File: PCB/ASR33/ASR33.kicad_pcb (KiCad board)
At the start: 2 copper layers, 45 x 27 mm, 44 parts, among them J1 Shelly, J2 DC, J3 Power, J4 RUN, J5 Tx, J6 Rx, J7 USB-C, Q1 NX7002AK, SW1 SW_Push, U1 ESP32-PICO-MINI-02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

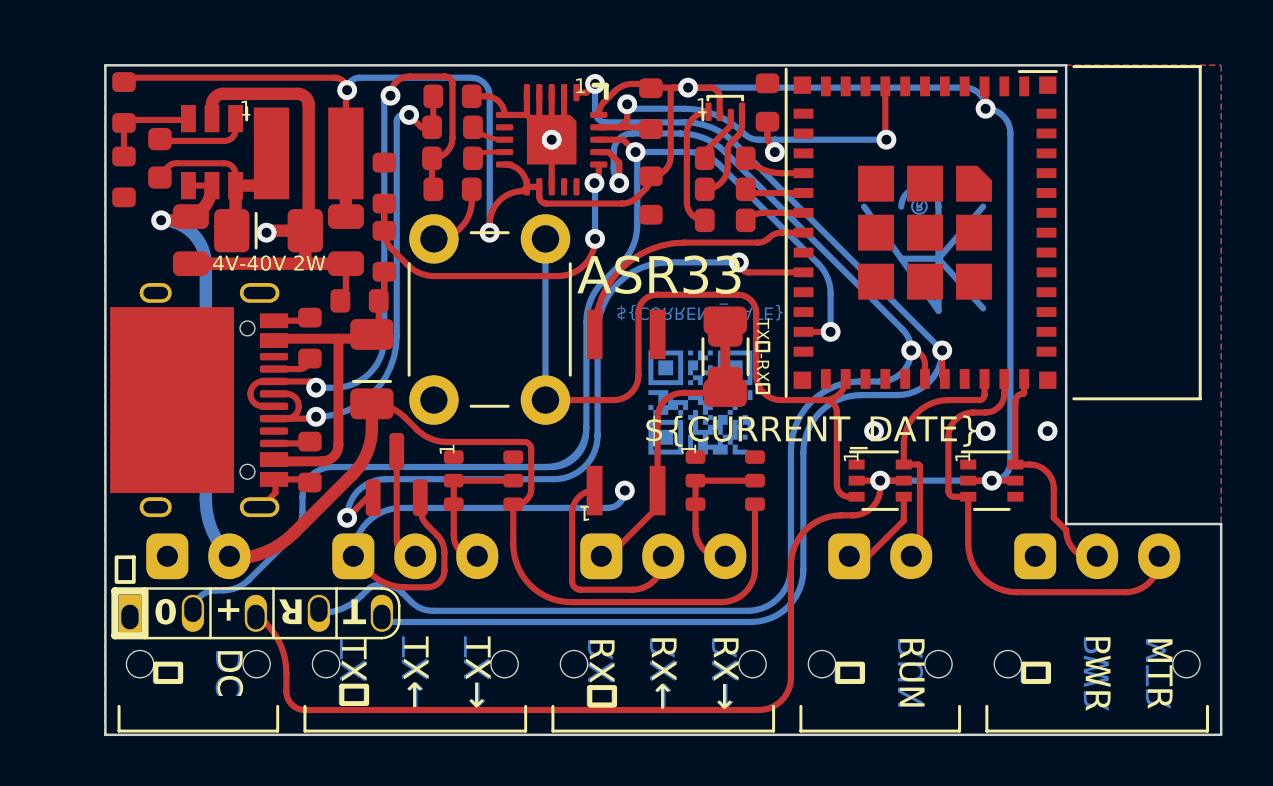
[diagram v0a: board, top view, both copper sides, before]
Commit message: New layout with S3
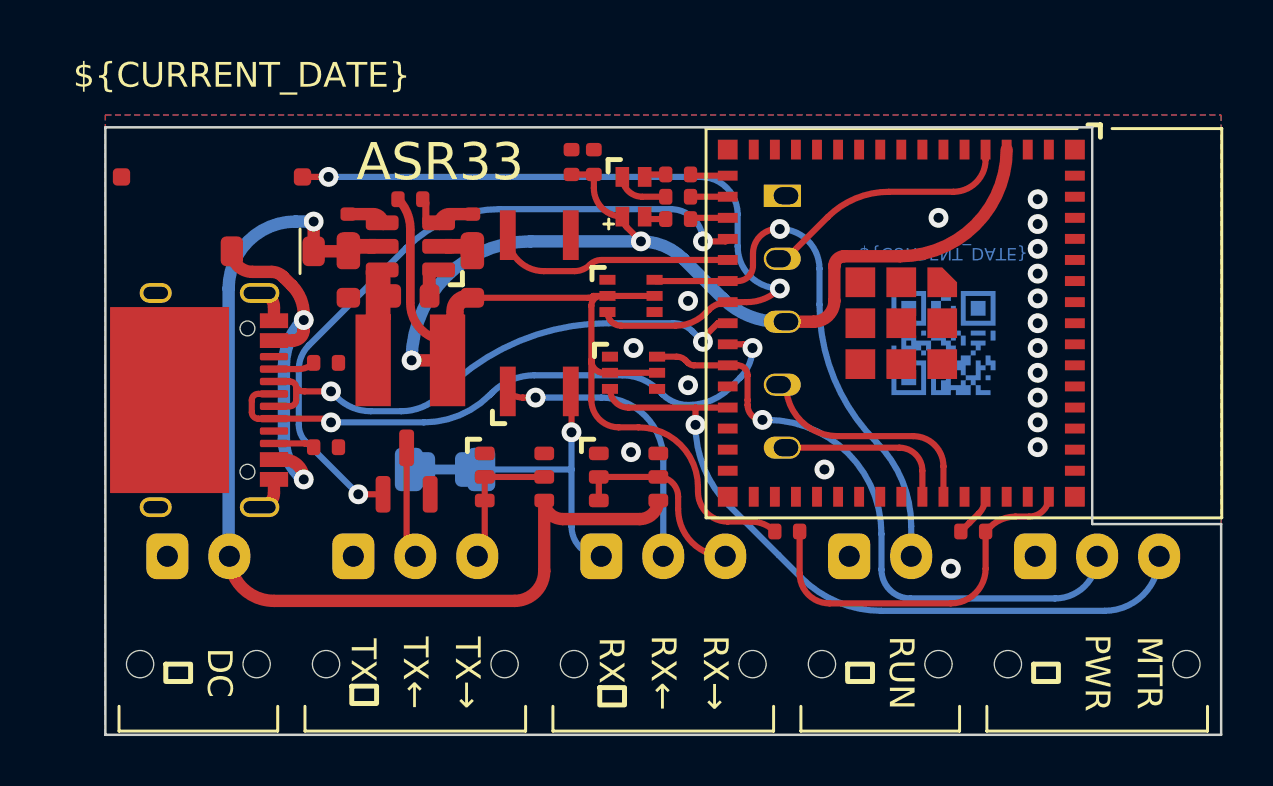
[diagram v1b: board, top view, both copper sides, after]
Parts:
- removed C2, C3: 47pF, RevK:C_0603
- removed C4: 10nF, RevK:C_0603
- removed C5: 100nF, RevK:C_0603_
- removed C6: 2.2uF, RevK:C_0805_
- removed C7: 10uF, RevK:C_0805_
- removed D4: Schottky, RevK:D_1206
- removed J1: Shelly, RevK:Shelly
- removed L1: 6.8uH, RevK:L_4x4_
- removed Logo1: AJK, RevK:AJK
- removed R10, R9: 27R, RevK:R_0603
- removed R4: 300R, RevK:R_0603
- removed R5: 1K, RevK:R_0603
- removed R6: 100R, RevK:R_0603
- removed U2: FT231XQ, RevK:QFN-20-1EP_4x4mm_P0.5mm_EP2.5x2.5mm
- removed U6: LMR16006XDDCR, RevK:SOT-23-Thin-6-Reg
- added C10: 22uF, RevK:C_0402, F.Cu at (138.8, 97.4)
- added C11: 1uF, RevK:C_0402, F.Cu at (155.0, 112.3)
- added C12: 100nF, RevK:C_0603_, F.Cu at (132.3, 102.8)
- added C9: 100nF, RevK:C_0402, F.Cu at (139.7, 97.4)
- added J8: Shelly, RevK:Shelly, B.Cu at (147.3, 103.8)
- added L2: 10uH, RevK:L_4x4_, F.Cu at (132.3, 105.4)
- added R13: 10K, RevK:R_0402, F.Cu at (147.5, 112.3)
- added R14: 220R, RevK:R_0402, F.Cu at (143.1, 99.7)
- added U8: ESP32-S3-MINI-1, RevK:ESP32-S3-MINI-1, F.Cu at (152.1, 103.9)
- C1: value 100nF -> 10uF 50V; footprint RevK:C_0603 -> RevK:C_0603_
- C8: value 1uF -> 10uF 6.3V; footprint RevK:C_0603 -> RevK:C_0603_
- D1: value LED_BARG -> D; footprint RevK:MHS190RGBCT -> RevK:D_SOD-123
- D2, D3: footprint Package_TO_SOT_SMD:SOT-363_SC-70-6 -> RevK:SOT-363_SC-70-6
- D5: value Schottky -> RGB; footprint RevK:D_1206_ -> RevK:LED-RGB-1.6x1.6
- JP1: moved to B.Cu
- R1: value 10k -> 124k; footprint RevK:R_0603 -> RevK:R_0402_
- R11: value 100k 1% -> 680R; footprint RevK:R_0603 -> RevK:R_0402
- R12: value 30k 1% -> 2K; footprint RevK:R_0603 -> RevK:R_0402
- R2: value 4k7 -> 39k2; footprint RevK:R_0603 -> RevK:R_0402_
- R3: value 10k -> 1M; footprint RevK:R_0603 -> RevK:R_0402_
- R7, R8: footprint RevK:R_0603 -> RevK:R_0402
- SW1: footprint RevK:SW_PUSH_6mm_PTH -> RevK:TS-1092S-B3D2-G
- U1: value ESP32-PICO-MINI-02 -> MD8942; footprint RevK:ESP32-PICO-MINI-02 -> RevK:SOT-23-6-MD8942
- moved R11 22.7 mm to (143.1, 98.8), turned to 0 degrees
- moved R12 22.4 mm to (143.1, 97.9), turned to 0 degrees
- moved U1 20.8 mm to (132.3, 100.8), turned to 0 degrees
- moved D1 19.1 mm to (126.8, 101.0), turned to 180 degrees
- moved D2 15.1 mm to (141.3, 105.9)
- moved D5 14.8 mm to (141.3, 98.8), turned to -90 degrees
- moved C8 13.9 mm to (134.8, 102.1), turned to 90 degrees
- moved C1 12.7 mm to (129.8, 102.1), turned to 90 degrees
- moved SW1 12.6 mm to (124.3, 98.0), turned to 0 degrees
- moved D3 12.5 mm to (141.2, 102.8)
- moved JP1 12.2 mm to (133.7, 109.8), turned to 0 degrees
- moved R1 10.4 mm to (132.3, 98.9), turned to 0 degrees
- moved U7 10.1 mm to (153.8, 104.7)
- moved U5 5.32 mm to (137.5, 103.5)
- moved U4 3.90 mm to (141.1, 110.1)
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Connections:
- D1 pad 1: Net-(D1-BK) -> DC
- D1 pad 2: +3V3 -> VBUS
- J7 pad A6: Net-(C3-Pad1) -> D+
- J7 pad A7: Net-(C2-Pad1) -> D-
- J7 pad B6: Net-(C3-Pad1) -> D+
- J7 pad B7: Net-(C2-Pad1) -> D-
- R11 pad 1: +3V3 -> Net-(D5-RK)
- R11 pad 2: Net-(U6-FB) -> R
- R12 pad 1: GND -> Net-(D5-GK)
- R12 pad 2: Net-(U6-FB) -> G
- U1 pad 1: GND -> unconnected-(U1-Pad1)
- U1 pad 3: +3V3 -> unconnected-(U1-Pad3)
- U1 pad 5: unconnected-(U1-I37-Pad5) -> DC
- U1 pad 7: unconnected-(U1-I39-Pad7) -> GND
- U1 pad 8: EN -> +3V3
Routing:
- net +3V3: track 117.4 -> 63.0 mm, vias 6 -> 2
- net I: track 53.0 -> 0.00 mm, vias 2 -> 0
- net O: track 51.4 -> 0.00 mm, vias 2 -> 0
- net GPIO0: track 50.6 -> 0.00 mm, vias 2 -> 0
- net GND: track 44.5 -> 4.62 mm, vias 6 -> 18
- net Net-(C2-Pad1): track 25.7 -> 0.00 mm, vias 2 -> 0
- net D+: track 1.33 -> 24.9 mm, vias 0 -> 2
- net Net-(C3-Pad1): track 20.7 -> 0.00 mm, vias 2 -> 0
- net D-: track 1.34 -> 21.8 mm, vias 0 -> 2
- net EN: track 17.9 -> 0.00 mm, vias 3 -> 0
- net PWR: track 9.35 -> 25.0 mm, vias 0 -> 1
- net Net-(U8-EN): track 0.00 -> 15.2 mm
- net Net-(U2-CBUS3): track 14.4 -> 0.00 mm, vias 2 -> 0
- net RUN: track 9.83 -> 21.3 mm, vias 0 -> 1
- net MTR: track 18.2 -> 29.5 mm, vias 0 -> 1
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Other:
- board size 45 x 27 mm -> 45 x 24.5 mm
- board text added: "15"
- board text added: "16"
- board text added: "17"
- board text added: "18"
- board text added: "47"
- board text added: "A"
- board text added: "B"
- board text added: "RGB: 13/2/14"
- board text added: "USB 5V, or 5V-36V DC"
- board text removed: "13"
- board text removed: "14"
- board text removed: "19"
- board text removed: "20"
- board text removed: "22"
- board text removed: "RGB: 25/26/27"
- board text removed: "USB 5V, or 4V-40V DC"

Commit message: iTidy
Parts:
- moved R2 1.30 mm to (134.1, 98.9), turned to 0 degrees
- moved R3 1.30 mm to (130.5, 98.9), turned to 0 degrees
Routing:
- net TX20MA: track 27.7 -> 31.5 mm
- net DC: track 40.9 -> 42.7 mm

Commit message: Clean up PCB
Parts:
- removed D5: RGB, RevK:LED-RGB-1.6x1.6
- removed R11: 680R, RevK:R_0402
- removed R12: 2K, RevK:R_0402
- removed R14: 220R, RevK:R_0402
- added D4: XL-1010RGBC-WS2812B, RevK:SMD1010, F.Cu at (98.9, 86.0)
- added D6: ~, RevK:DFN1006-2L, F.Cu at (99.5, 95.2)
- added D7: ~, RevK:DFN1006-2L, F.Cu at (99.5, 90.3)
- added PCB1: 70x70, RevK:PCB7070, F.Cu at (100.0, 100.0)
- added V1: ~, RevK:VCUT70N, F.Cu at (100.0, 84.0)
- added V2: ~, RevK:VCUT70N, F.Cu at (100.0, 108.5)
- added V3: ~, RevK:VCUT70N, F.Cu at (76.5, 100.0)
- added V4: ~, RevK:VCUT70N, F.Cu at (121.0, 100.0)
- D2, D3: value BAV99S -> ~; footprint RevK:SOT-363_SC-70-6 -> RevK:DFN1006-2L
- J7: value USB-C -> USB-C-Socket-V; footprint RevK:USC16-TR -> RevK:USB-C-Socket-H
- moved C1 45.4 mm to (86.0, 90.2)
- moved C10 45.4 mm to (95.0, 85.5)
- moved C12 45.4 mm to (88.5, 90.9)
- moved C8 45.4 mm to (91.0, 90.2)
- moved J8 45.4 mm to (103.5, 91.9)
- moved L2 45.4 mm to (88.5, 93.5)
- moved Q1 45.4 mm to (88.3, 98.0)
- moved R1 45.4 mm to (88.5, 87.0)
- moved R7 45.4 mm to (85.1, 93.6)
- moved R8 45.4 mm to (85.1, 97.0)
- moved U1 45.4 mm to (88.5, 88.9)
- moved U7 45.4 mm to (110.0, 92.8)
- moved C11 45.4 mm to (111.2, 100.4)
- moved D1 45.4 mm to (83.0, 89.1)
- moved J2 45.4 mm to (80.0, 101.4)
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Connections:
- D2 pad 1: GND -> BUTTON
- D2 pad 2: +3V3 -> GND
- D3 pad 1: GND -> PWR
- D3 pad 2: +3V3 -> GND
- U8 pad 16: G -> RGB
- U8 pad 17: R -> unconnected-(U8-GPIO13-Pad17)
- U8 pad 18: B -> unconnected-(U8-GPIO14-Pad18)
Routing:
- net +3V3: track 63.0 -> 54.8 mm, vias 2 -> 3
- net GND: track 4.62 -> 10.2 mm, vias 18 -> 15
- net BUTTON: track 29.9 -> 25.8 mm
- net MTR: track 29.5 -> 25.6 mm
- net Net-(D5-RK): track 2.17 -> 0.00 mm
- net RGB: track 0.00 -> 1.80 mm
- net PWR: track 25.0 -> 23.4 mm
- net RUN: track 21.3 -> 19.7 mm
- net R: track 1.50 -> 0.00 mm
- net G: track 1.45 -> 0.00 mm
- net B: track 1.45 -> 0.00 mm
- net Net-(D5-GK): track 0.75 -> 0.00 mm
- net Net-(D5-BK): track 0.75 -> 0.00 mm
- net D+: track 24.9 -> 24.2 mm
- net RX20MA: track 9.75 -> 10.3 mm
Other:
- board size 45 x 24.5 mm -> 70 x 70 mm
- board text added: "RGB:12"
- board text removed: "RGB: 13/2/14"

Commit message: Tweak
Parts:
- C1: value 10uF 50V -> 10uF 35V

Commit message: Tidy
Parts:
- D4: footprint RevK:SMD1010 -> RevK:SMD1010+
- moved D2 0.45 mm to (99.1, 91.2)
- moved D3 0.45 mm to (99.1, 93.7)
- moved D4 0.45 mm to (98.5, 86.0)
- moved D6 0.45 mm to (99.1, 95.2)
- moved D7 0.45 mm to (99.1, 90.3)
- moved J8 0.45 mm to (103.0, 91.9)
- moved U8 0.45 mm to (107.8, 92.0)
- moved SW1 0.30 mm to (80.8, 86.1)
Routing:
- net D+: track 24.2 -> 21.5 mm
- net Net-(J8-Rx): track 9.32 -> 10.3 mm
- net D-: track 21.7 -> 20.9 mm
- net GND: track 10.2 -> 9.38 mm, vias 15 -> 17
- net Net-(J8-Tx): track 7.34 -> 6.57 mm
- net +3V3: track 54.8 -> 54.2 mm
- net TX20MA: track 31.5 -> 30.8 mm
